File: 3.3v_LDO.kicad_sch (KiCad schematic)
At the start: 1 part

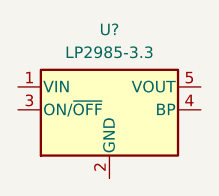
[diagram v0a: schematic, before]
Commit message: Clean up SMPS schematic
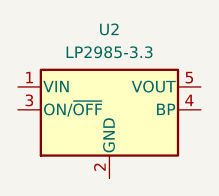
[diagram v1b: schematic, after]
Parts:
- gave numbers to parts that had none: 1
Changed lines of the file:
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@@
 		(dnp no)
 		(fields_autoplaced yes)
-		(property "Reference" "U?"
+		(property "Reference" "U2"
 			(at 128.27 68.58 0)
 			(effects
@@
 			(project ""
 				(path "/4d632659-7d2f-4407-ada5-b4e72f7be845/433705c3-0c9b-4b35-8329-f110f6531cb8"
-					(reference "U?")
+					(reference "U2")
 					(unit 1)
 				)

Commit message: Ross Added branch
added a branch
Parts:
- removed U2: LP2985-3.3, Package_TO_SOT_SMD:SOT-23-5, symbol Regulator_Linear:LP2985-3.3
- added C?: 10 nF, symbol Device:C
- added C?: 2.2 µF, symbol Device:C
- added C?: 1 µF, symbol Device:C
- added TP?: TP_VIN, symbol Connector:TestPoint
- added TP?: TP_VOUT, symbol Connector:TestPoint
- added TP_BP?: TP4, symbol Connector:TestPoint
- added TP_EN?: TP2, symbol Connector:TestPoint
- added TP_GND?: TP3, symbol Connector:TestPoint
- added U?: LP2985-3.3, Package_TO_SOT_SMD:SOT-23-5, symbol Regulator_Linear:LP2985-3.3
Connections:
- new net: C?.1, TP?.1, TP_EN?.1, U?.1 (VIN), U?.3 (ON/~{OFF})
- new net: C?.1, TP_BP?.1, U?.4 (BP)
- new net: C?.1, TP?.1, U?.5 (VOUT)
- new net GND: C?.2, C?.2, C?.2, TP_GND?.1, U?.2 (GND)
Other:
- note added: "BYPASS"
- note added: "VIN"
- note added: "VOUT"

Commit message: Add LDO schematic + layout
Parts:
- removed C?: 10 nF, symbol Device:C
- removed C?: 2.2 µF, symbol Device:C
- removed C?: 1 µF, symbol Device:C
- removed TP?: TP_VIN, symbol Connector:TestPoint
- removed TP?: TP_VOUT, symbol Connector:TestPoint
- removed TP_BP?: TP4, symbol Connector:TestPoint
- removed TP_EN?: TP2, symbol Connector:TestPoint
- removed TP_GND?: TP3, symbol Connector:TestPoint
- added C17: 1u, Capacitor_SMD:C_0603_1608Metric, symbol Device:C
- added C18: 10n, Capacitor_SMD:C_0402_1005Metric, symbol Device:C
- added C19: 4.7u, Capacitor_SMD:C_0603_1608Metric, symbol Device:C
- added R5: 0, Resistor_SMD:R_0603_1608Metric, symbol Device:R
- added TP1: LDO_IN, TestPoint:TestPoint_THTPad_D1.0mm_Drill0.5mm, symbol Connector:TestPoint
- added TP2: ON/OFF, TestPoint:TestPoint_THTPad_D1.0mm_Drill0.5mm, symbol Connector:TestPoint
- gave numbers to parts that had none: 1
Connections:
- net GND: now also C17.2, C18.2, C19.2
- net ON/~{OFF}: now reaches U2.3 (ON/~{OFF})
- net ON/~{OFF}: now also R5.1, TP2.1; no longer U2.1 (VIN)
- net BP: now reaches U2.4 (BP)
- net BP: now also C18.1
- net 3V3_OUTPUT: now reaches U2.5 (VOUT)
- net 3V3_OUTPUT: now also C19.1
- new net VBAT+: C17.1, R5.2, TP1.1, U2.1 (VIN)
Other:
- note added: "2.2u new. 4.7u legacy"
- note removed: "BYPASS"
- note removed: "VIN"
- note removed: "VOUT"

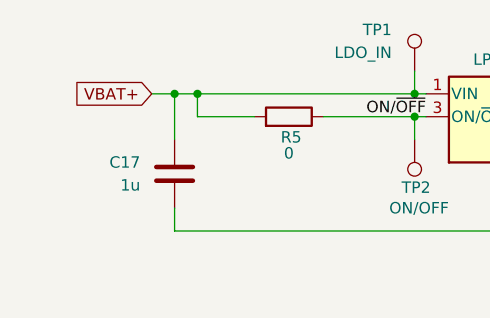
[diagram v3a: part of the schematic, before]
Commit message: rewire LDO input to 5V from VBAT and verify DRC
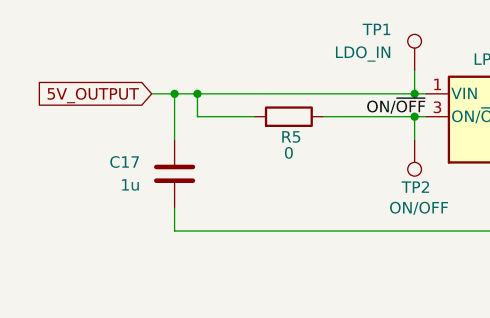
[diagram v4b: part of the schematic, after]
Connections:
- net VBAT+ renamed 5V_OUTPUT
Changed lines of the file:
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@@
+		)
+	)
+	(global_label "5V_OUTPUT"
+		(shape input)
+		(at 101.6 88.9 180)
+		(fields_autoplaced yes)
+		(effects
+			(font
+				(size 1.27 1.27)
+			)
+			(justify right)
+		)
+		(property "Intersheetrefs" "${INTERSHEET_REFS}"
+			(at 88.1524 88.9 0)
+			(effects
+				(font
+					(size 1.27 1.27)
+				)
+				(justify right)
+				(hide yes)
+			)
 		)
 	)
@@
 				(hide yes)
 			)
-		)
-	)
-	(global_label "VBAT+"
-		(shape input)
-		(at 101.6 88.9 180)
-		(fields_autoplaced yes)
-		(effects
-			(font
-				(size 1.27 1.27)
-			)
-			(justify right)
-		)
-		(property "Intersheetrefs" "${INTERSHEET_REFS}"
-			(at 92.6276 88.9 0)
-			(effects
-				(font
-					(size 1.27 1.27)
-				)
-				(justify right)
-				(hide yes)
-			)
